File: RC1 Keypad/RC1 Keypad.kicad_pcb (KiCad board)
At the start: 2 copper layers, 73 x 122.6 mm, 26 parts, among them J1 KB, SW1 Ø, SW10 3, SW11 A, SW12 DA, SW13 4, SW14 B, SW15 +, SW16 5, SW17 C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

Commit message: Keypad SX layout done
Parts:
- added M1: Mounting, Mounting:1pin, F.Cu at (91.4, 58.4)
- added M2: Mounting, Mounting:1pin, F.Cu at (151.1, 58.4)
- added M3: Mounting, Mounting:1pin, F.Cu at (91.4, 128.3)
- added M4: Mounting, Mounting:1pin, F.Cu at (151.1, 128.3)
- SW1, SW10, SW11, SW12, SW13, SW14, SW15, SW16, SW17, SW18, SW19, SW2, SW20, SW21, SW23, SW24, SW3, SW4, SW5, SW6, SW7, SW8, SW9: footprint Button_Switch_Keyboard:SW_Cherry_MX_1.00u_PCB -> Buttons_Switches_THT:SW_PUSH_6mm
- SW22: footprint Buttons_Switches_THT:SW_DIP_x1_W7.62mm_Slide -> Pin_Headers:Pin_Header_Straight_1x03_Pitch2.54mm
- moved SW10 46.2 mm to (136.5, 122.6)
- moved SW7 44.2 mm to (123.8, 122.6)
- moved SW1 43.4 mm to (98.4, 122.6)
- moved SW4 43.3 mm to (111.1, 122.6)
- moved SW2 38.1 mm to (136.5, 111.8)
- moved SW19 35.6 mm to (123.8, 111.8)
- moved SW13 34.6 mm to (98.4, 111.8)
- moved SW16 34.4 mm to (111.1, 111.8)
- moved SW14 30.3 mm to (136.5, 101.0)
- moved SW11 27.1 mm to (123.8, 101.0)
- moved SW5 25.8 mm to (98.4, 101.0)
- moved SW8 25.5 mm to (111.1, 101.0)
- moved SW6 23.3 mm to (136.5, 90.2)
- moved SW3 19.1 mm to (123.8, 90.2)
- moved SW15 18.8 mm to (136.5, 78.1)
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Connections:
- net /2A0 renamed /PA0
- net /2A1 renamed /PA1
- net /2A2 renamed /PA2
- net /2A3 renamed /PA3
- net /2A4 renamed /PA4
- net /2A5 renamed /PA5
- net /2A6 renamed /PA6
- net /ROW_0 renamed /ROW2
- net /ROW_1 renamed /ROW1
- net /ROW_2 renamed /ROW0
- SW22 pad 1: /SST_IN -> (no net)
- SW22 pad 2: /SST_OUT -> /SST_IN
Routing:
- net /PA4: track 189.3 -> 114.0 mm
- net /PA5: track 201.3 -> 133.3 mm, vias 1 -> 2
- net /PA3: track 161.7 -> 97.9 mm, vias 1 -> 2
- net /ROW0: track 212.8 -> 149.4 mm, vias 2 -> 1
- net /PA6: track 193.5 -> 136.4 mm, vias 3 -> 0
- net /PA0: track 129.5 -> 85.8 mm
- net /PA2: track 177.9 -> 135.3 mm
- net /ROW1: track 182.7 -> 141.2 mm
- net /PA1: track 132.6 -> 101.8 mm
- net /SST_IN: track 44.4 -> 17.6 mm, vias 0 -> 1
- net /ST: track 18.9 -> 36.4 mm, vias 0 -> 1
- net /SST_OUT: track 34.1 -> 20.1 mm, vias 0 -> 1
- net /ROW2: track 138.2 -> 129.7 mm
- net /LED: track 29.5 -> 21.0 mm, vias 1 -> 0
- net /RS: track 52.5 -> 45.4 mm
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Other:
- board size 73 x 122.6 mm -> 66 x 76.2 mm
- board text added: "Keypad Revision A"
- board text added: "RC-ONE"
- board text added: "github.com/tebl"

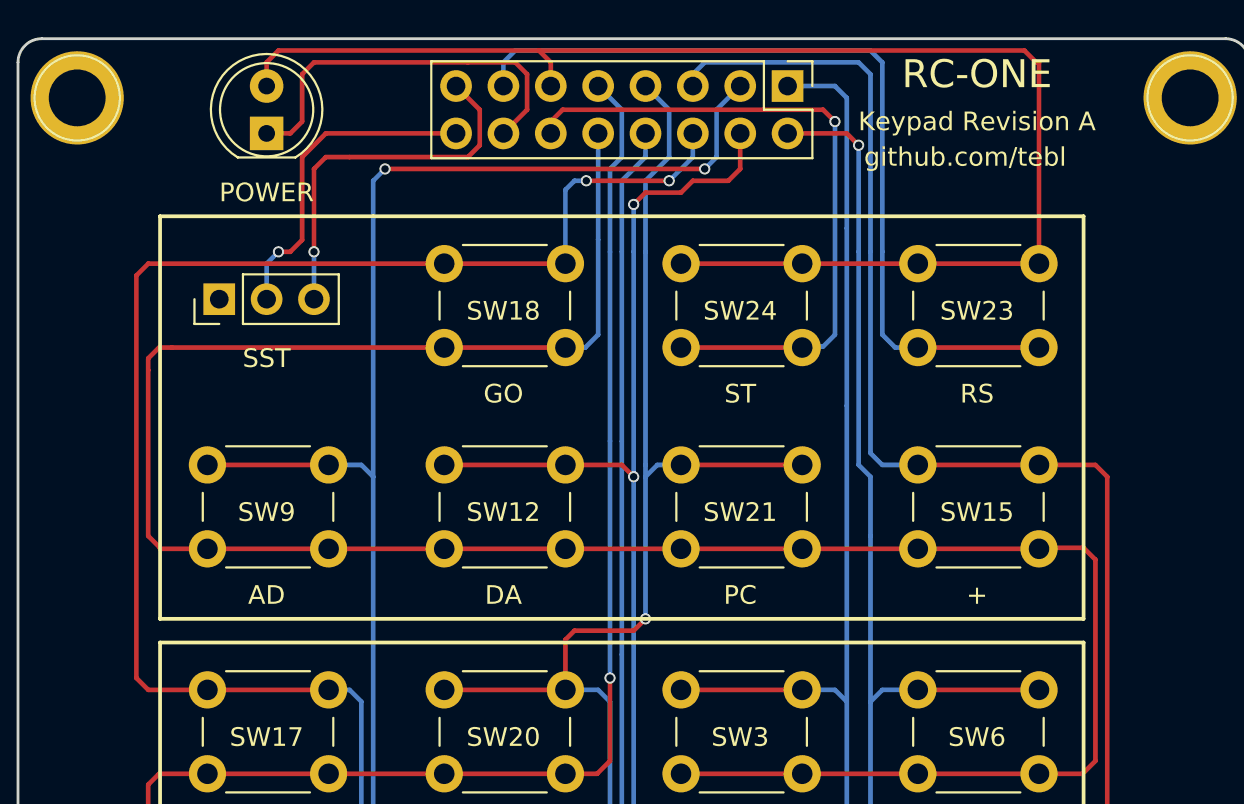
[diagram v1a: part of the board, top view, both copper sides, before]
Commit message: Keypad SST moved to match original keypad layout
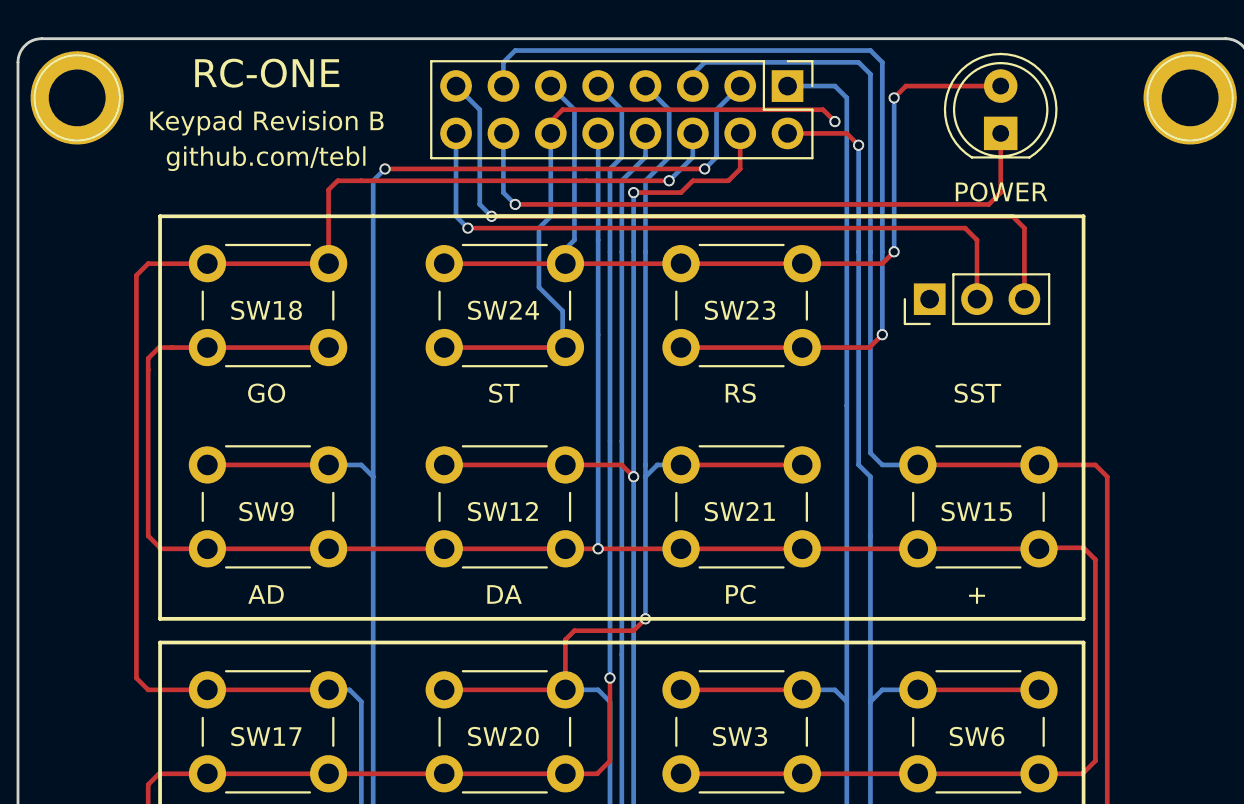
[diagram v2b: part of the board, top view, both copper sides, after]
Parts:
- moved D1 39.4 mm to (141.0, 60.3)
- moved SW22 38.1 mm to (137.2, 69.2)
- moved SW18 12.7 mm to (98.4, 67.3)
- moved SW23 12.7 mm to (123.8, 67.3)
- moved SW24 12.7 mm to (111.1, 67.3)
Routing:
- net /VCC: track 75.4 -> 48.9 mm, vias 0 -> 2
- net /SST_OUT: track 20.1 -> 40.4 mm
- net /SST_IN: track 17.6 -> 36.1 mm
- net /LED: track 21.0 -> 33.5 mm, vias 0 -> 1
- net /ROW2: track 129.7 -> 126.4 mm, vias 0 -> 1
- net /RS: track 45.4 -> 47.8 mm, vias 0 -> 1
- net /ST: track 36.4 -> 35.2 mm
- net /PA1: vias 2 -> 1
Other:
- board text added: "Keypad Revision B"
- board text removed: "Keypad Revision A"

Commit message: Updated keypad schematic for clarity
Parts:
- J1: value KB -> KEYPAD
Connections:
- net /LED renamed Net-(D1-Pad1)
- net /RS renamed Net-(J1-Pad13)
- net /SST_IN renamed Net-(J1-Pad16)
- net /SST_OUT renamed Net-(J1-Pad15)
- net /ST renamed Net-(J1-Pad12)
- net /VCC renamed Net-(D1-Pad2)
